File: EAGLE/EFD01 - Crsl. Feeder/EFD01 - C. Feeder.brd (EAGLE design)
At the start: 50 x 50 mm, 35 parts, among them J1 MOD TOOL, J2 SPI, J3 MOT, J4 FTDI, Q1 BSS138, Q2 16MHz, U1 SP3485, U2 TCST1030, U3 ATMEGA238, U4 DRV8825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

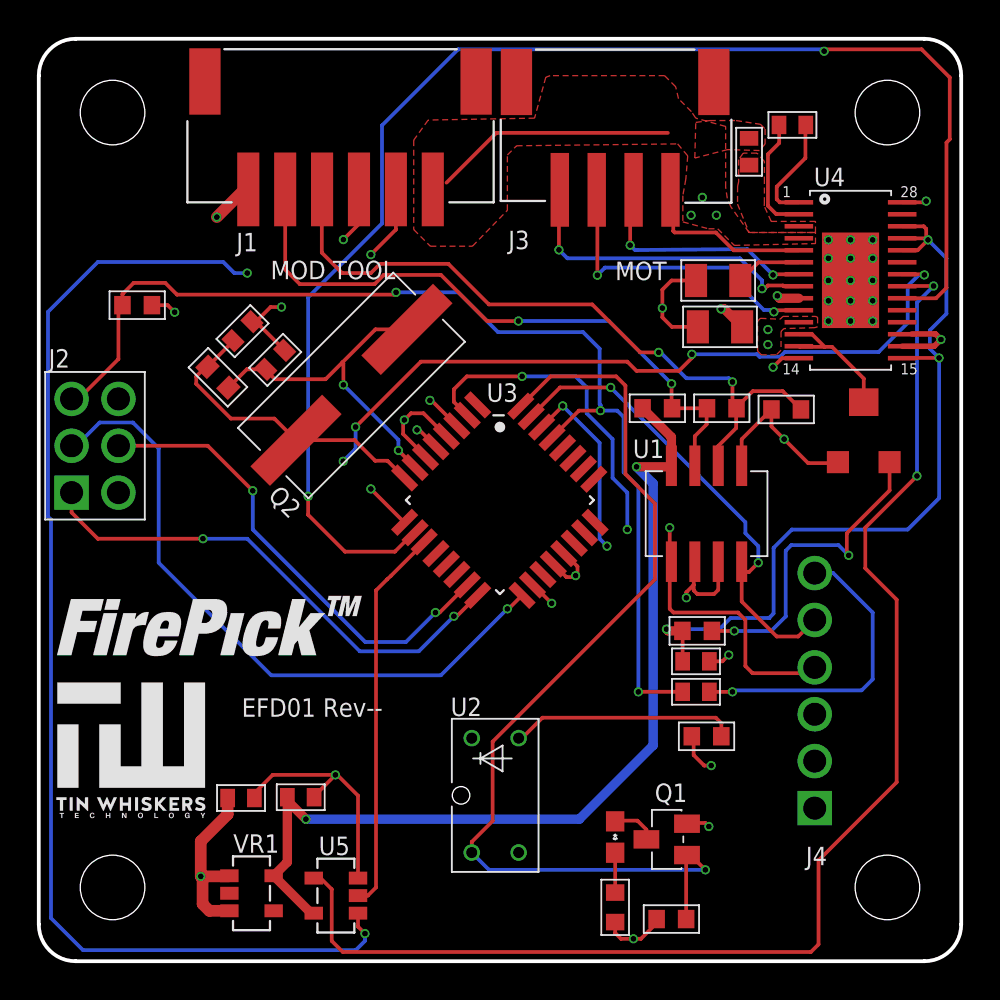
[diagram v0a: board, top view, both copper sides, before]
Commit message: Fixed BOM, began adding DFM changes
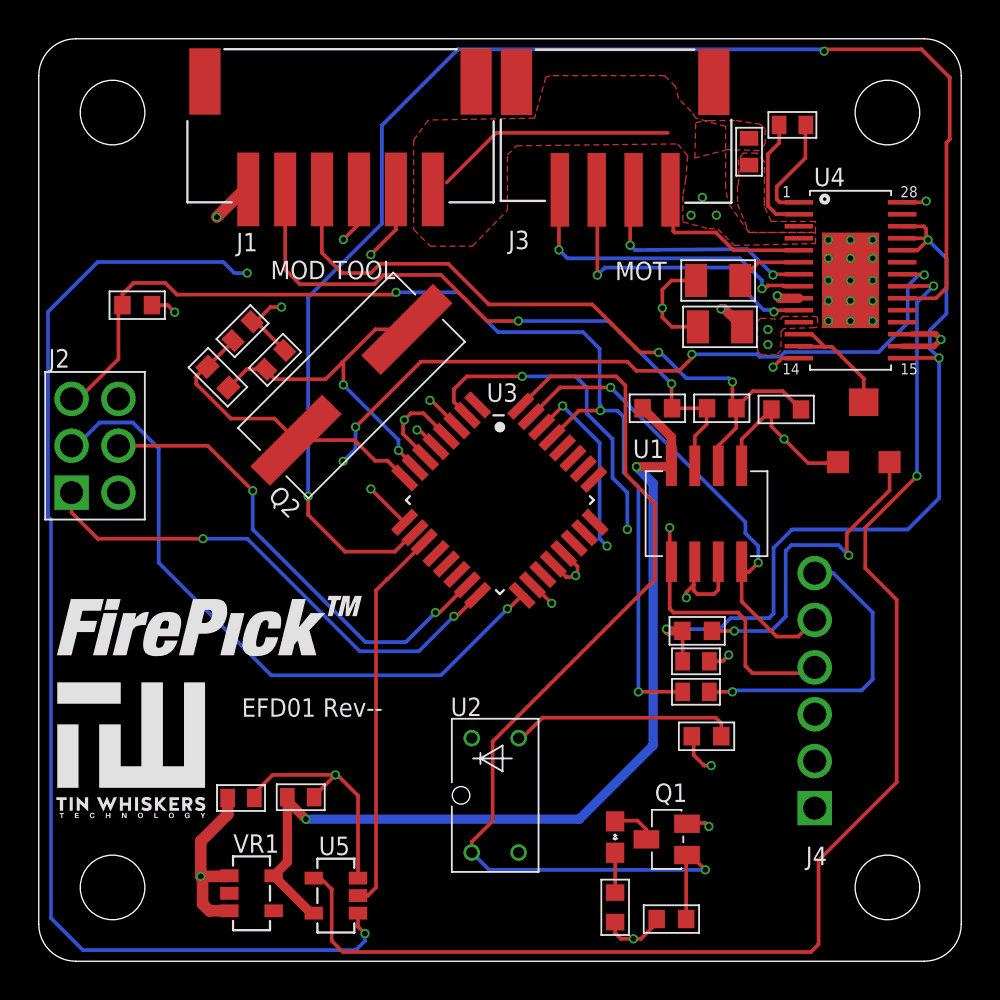
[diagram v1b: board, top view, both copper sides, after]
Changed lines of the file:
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@@
 <?xml version="1.0" encoding="utf-8"?>
 <!DOCTYPE eagle SYSTEM "eagle.dtd">
-<eagle version="7.3.0">
+<eagle version="7.4.0">
 <drawing>
 <settings>
@@
 <grid distance="0.25" unitdist="mm" unit="mm" style="lines" multiple="1" display="yes" altdistance="0.001" altunitdist="inch" altunit="inch"/>
 <layers>
-<layer number="1" name="Top" color="4" fill="1" visible="no" active="yes"/>
-<layer number="2" name="Route2" color="1" fill="3" visible="no" active="yes"/>
+<layer number="1" name="Top" color="4" fill="1" visible="yes" active="yes"/>
+<layer number="2" name="Route2" color="1" fill="3" visible="yes" active="yes"/>
 <layer number="3" name="Route3" color="4" fill="3" visible="no" active="no"/>
 <layer number="4" name="Route4" color="1" fill="4" visible="no" active="no"/>
@@
 <layer number="13" name="Route13" color="4" fill="5" visible="no" active="no"/>
 <layer number="14" name="Route14" color="1" fill="6" visible="no" active="no"/>
-<layer number="15" name="Route15" color="4" fill="6" visible="no" active="yes"/>
-<layer number="16" name="Bottom" color="1" fill="1" visible="no" active="yes"/>
+<layer number="15" name="Route15" color="4" fill="6" visible="yes" active="yes"/>
+<layer number="16" name="Bottom" color="1" fill="1" visible="yes" active="yes"/>
 <layer number="17" name="Pads" color="2" fill="1" visible="yes" active="yes"/>
 <layer number="18" name="Vias" color="2" fill="1" visible="yes" active="yes"/>
@@
 <layer number="20" name="Dimension" color="15" fill="1" visible="yes" active="yes"/>
 <layer number="21" name="tPlace" color="7" fill="1" visible="yes" active="yes"/>
-<layer number="22" name="bPlace" color="7" fill="1" visible="no" active="yes"/>
-<layer number="23" name="tOrigins" color="15" fill="1" visible="no" active="yes"/>
-<layer number="24" name="bOrigins" color="15" fill="1" visible="no" active="yes"/>
+<layer number="22" name="bPlace" color="7" fill="1" visible="yes" active="yes"/>
+<layer number="23" name="tOrigins" color="15" fill="1" visible="yes" active="yes"/>
+<layer number="24" name="bOrigins" color="15" fill="1" visible="yes" active="yes"/>
 <layer number="25" name="tNames" color="7" fill="1" visible="yes" active="yes"/>
-<layer number="26" name="bNames" color="7" fill="1" visible="no" active="yes"/>
+<layer number="26" name="bNames" color="7" fill="1" visible="yes" active="yes"/>
 <layer number="27" name="tValues" color="7" fill="1" visible="no" active="yes"/>
 <layer number="28" name="bValues" color="7" fill="1" visible="no" active="yes"/>
-<layer number="29" name="tStop" color="7" fill="3" visible="no" active="yes"/>
-<layer number="30" name="bStop" color="7" fill="6" visible="no" active="yes"/>
+<layer number="29" name="tStop" color="7" fill="3" visible="yes" active="yes"/>
+<layer number="30" name="bStop" color="7" fill="6" visible="yes" active="yes"/>
 <layer number="31" name="tCream" color="7" fill="4" visible="yes" active="yes"/>
-<layer number="32" name="bCream" color="7" fill="5" visible="no" active="yes"/>
+<layer number="32" name="bCream" color="7" fill="5" visible="yes" active="yes"/>
 <layer number="33" name="tFinish" color="6" fill="3" visible="no" active="yes"/>
 <layer number="34" name="bFinish" color="6" fill="6" visible="no" active="yes"/>
@@
 <board>
 <plain>
-<wire x1="2" y1="0" x2="48" y2="0" width="0.2032" layer="20"/>
-<wire x1="48" y1="0" x2="50" y2="2" width="0.2032" layer="20" curve="90"/>
-<wire x1="50" y1="2" x2="50" y2="48" width="0.2032" layer="20"/>
-<wire x1="48" y1="50" x2="2" y2="50" width="0.2032" layer="20"/>
-<wire x1="2" y1="50" x2="0" y2="48" width="0.2032" layer="20" curve="90"/>
-<wire x1="0" y1="48" x2="0" y2="2" width="0.2032" layer="20"/>
-<wire x1="0" y1="2" x2="2" y2="0" width="0.2032" layer="20" curve="90"/>
-<wire x1="50" y1="48" x2="48" y2="50" width="0.2032" layer="20" curve="90"/>
+<wire x1="2" y1="0" x2="48" y2="0" width="0" layer="20"/>
+<wire x1="48" y1="0" x2="50" y2="2" width="0" layer="20" curve="90"/>
+<wire x1="50" y1="2" x2="50" y2="48" width="0" layer="20"/>
+<wire x1="48" y1="50" x2="2" y2="50" width="0" layer="20"/>
+<wire x1="2" y1="50" x2="0" y2="48" width="0" layer="20" curve="90"/>
+<wire x1="0" y1="48" x2="0" y2="2" width="0" layer="20"/>
+<wire x1="0" y1="2" x2="2" y2="0" width="0" layer="20" curve="90"/>
+<wire x1="50" y1="48" x2="48" y2="50" width="0" layer="20" curve="90"/>
 <hole x="4" y="4" drill="3.5"/>
 <hole x="46" y="4" drill="3.5"/>

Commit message: Added decoupling caps to EFD01, ECAM02, rearranged parts for better fit, increased power trace width, updated BOM and database.
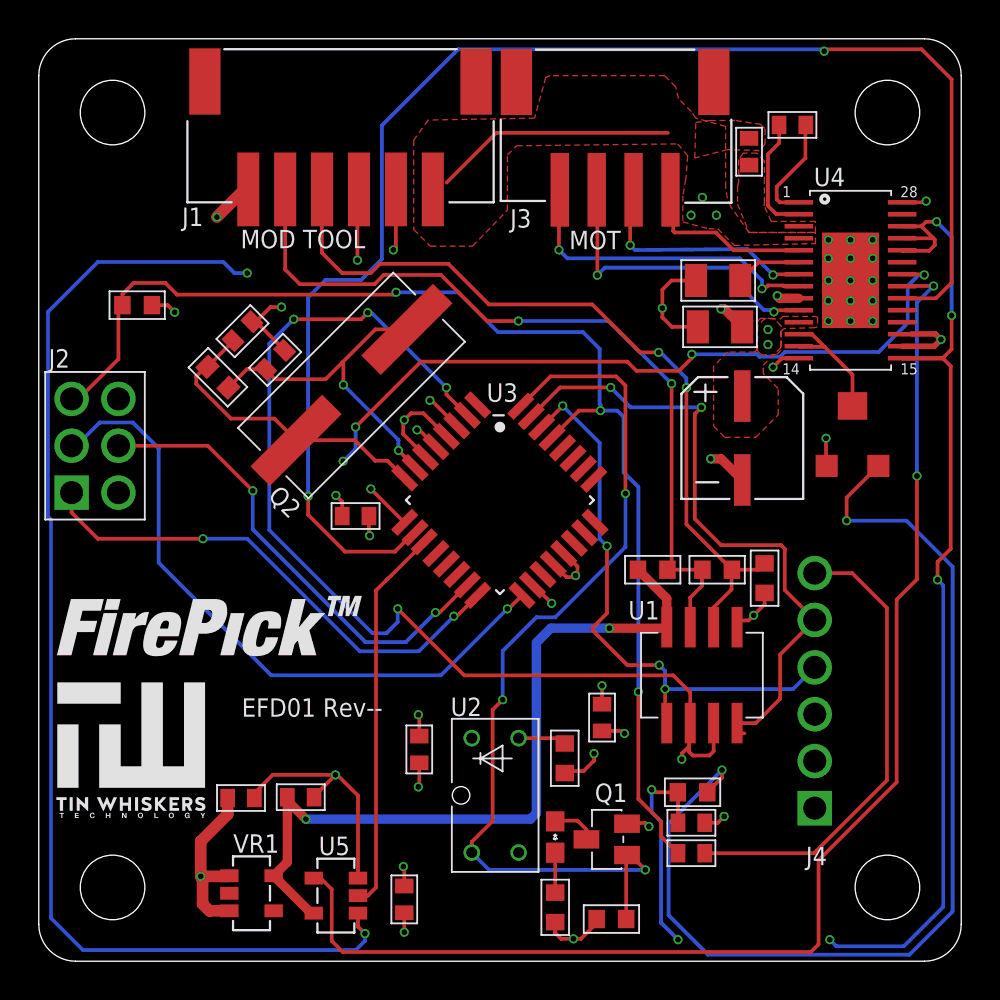
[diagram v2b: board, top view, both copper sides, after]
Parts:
- added C10, C11, C12, C13: 0.1uF, TinWhiskers:C0603
- added C9: 100uF, TinWhiskers:C-SMD-6.3MM
- moved R4 9.22 mm to (39.3, 20.8), turned to 90 degrees
- moved U1 8.75 mm to (35.9, 15.5)
- moved C3 8.75 mm to (35.4, 7.51)
- moved C6 8.75 mm to (35.4, 5.86)
- moved R2 8.75 mm to (36.8, 21.2)
- moved R3 8.75 mm to (33.3, 21.2)
- moved R7 8.75 mm to (35.4, 9.16)
- moved R10 7.78 mm to (28.5, 11.0), turned to 270 degrees
- moved LED1 3.25 mm to (28.0, 6.73)
- moved Q1 3.25 mm to (30.8, 6.60)
- moved R11 3.25 mm to (28.0, 2.92)
- moved R9 3.25 mm to (31.0, 2.29)
- moved R1 0.64 mm to (44.1, 28.6)
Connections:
- net +24V: now also C9.POS
- net +5V: now also C10.2, C11.2, C12.2, C13.2
- net GND: now also C10.1, C11.1, C12.1, C13.1, C9.NEG
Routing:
- net N$14: track 17.8 -> 57.0 mm
- net N$13: track 44.4 -> 76.8 mm, vias 3 -> 6
- net DTR1: track 29.6 -> 59.2 mm, vias 3 -> 5
- net N$2: track 12.3 -> 2.93 mm
- net DI: track 26.2 -> 35.5 mm
- net B: track 34.9 -> 43.7 mm
- net N$16: track 16.8 -> 25.6 mm, vias 1 -> 0
- net +3V3: track 50.8 -> 42.2 mm
- net RESET: track 60.4 -> 67.6 mm
- net A: track 38.4 -> 43.3 mm
- net +5V: track 30.5 -> 35.2 mm, vias 8 -> 12
- net O_OUT: track 54.5 -> 50.5 mm, vias 1 -> 3
- net GND: track 47.1 -> 49.9 mm, vias 27 -> 33
- net RO: track 29.4 -> 31.5 mm, vias 3 -> 4
- net !ENABLE: track 72.2 -> 70.8 mm
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
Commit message: Made REV 2 modifications, including increasing width of power traces, adding vias to power traces, and addition of LEDs to all modular tools. Catch diodes added to ESOL01 board to prevent coils from creating problems "upstream"
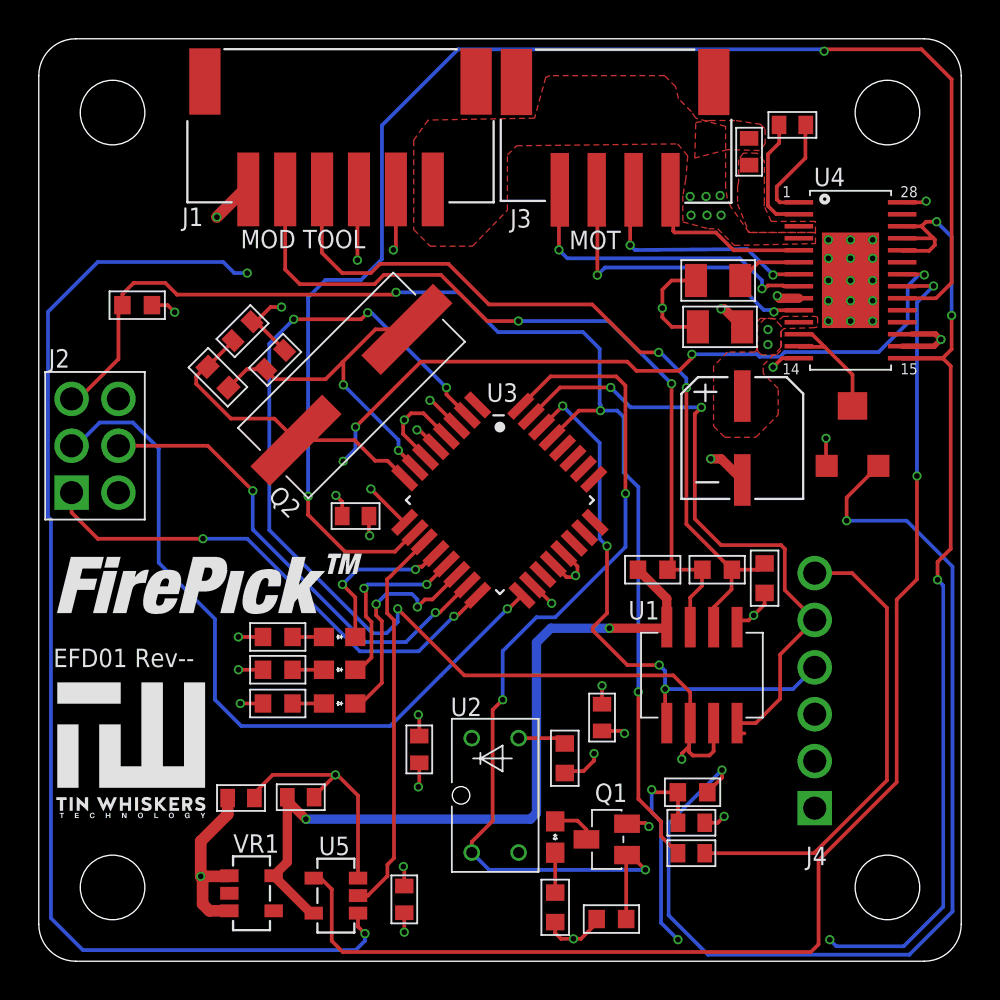
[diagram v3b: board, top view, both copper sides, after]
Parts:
- added LED2, LED3, LED4: RED, TinWhiskers:LED0603
- added R13, R14, R15: 1K, TinWhiskers:R0603
- moved LOGO2 2.29 mm to (0.79, 17.1)
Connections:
- new net N$10: LED2.A, R13.1
- new net N$11: LED3.C, U3.13
- new net N$12: LED3.A, R14.1
- new net N$17: LED4.C, U3.14
- new net N$18: LED4.A, R15.1
- new net N$7: LED2.C, U3.12
- net +5V: now also R13.2, R14.2, R15.2
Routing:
- net +24V: track 13.1 -> 0.02 mm, vias 5 -> 8
- net N$17: track 0.00 -> 12.2 mm, vias 0 -> 2
- net N$11: track 0.00 -> 10.1 mm, vias 0 -> 2
- net N$7: track 0.00 -> 8.90 mm, vias 0 -> 2
- net SCK: track 36.0 -> 40.9 mm
- net +5V: track 35.2 -> 39.1 mm, vias 12 -> 15
- net N$18: track 0.00 -> 1.70 mm
- net N$12: track 0.00 -> 1.70 mm
- net N$10: track 0.00 -> 1.70 mm
